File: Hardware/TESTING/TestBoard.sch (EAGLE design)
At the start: 91 parts, among them IC1 OP-AMP, J2 ISP, Q1 MOSFET_PCH-IRLML2244, U1 TAP_POINT, U10 MCP1755, U11 AD7280A, U12 ATMEGA328P_TQFP, U13 CH340C, U2 TAP_POINT, U3 TAP_POINT, U4 TAP_POINT, U5 TAP_POINT, U6 SINGLECELL, U7 SINGLECELL, U8 SINGLECELL, U9 SINGLECELL, Y1 16MHz

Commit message: Add spacious test board design
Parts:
- removed C14, C16, C17, C18, C20: 0.1uF, SparkFun-Capacitors:0.1UF-0603-25V-(+80/-20%)
- removed C19: 1.0uF, SparkFun-Capacitors:1.0UF-0603-16V-10%-X7R
- removed C21: 10nF, SparkFun-Capacitors:10NF-0603-50V-10%
- removed D8: BLUE, SparkFun-LED:LED-BLUE0603
- removed D9: 3A/10V/280mV, SparkFun-DiscreteSemi:DIODE-SCHOTTKY-BAT60A
- removed R33: 1k, SparkFun-Resistors:1KOHM-0603-1/10W-1%
- removed S2: TEST, SparkFun-Switches:MOMENTARY-SWITCH-SPST-SMD-5.2-TALL-REDUNDANT
- removed S3: Tall Switch, SparkFun-Switches:MOMENTARY-SWITCH-SPST-SMD-5.2-TALL-REDUNDANT
- removed U12: ATMEGA328P_TQFP, SparkFun-IC-Microcontroller:ATMEGA328P_TQFP
- removed U13: CH340C, SparkFun-IC-Comms:CH340C
- removed Y1: 16MHz, SparkFun-Clocks:RESONATOR-16MHZSMD_3.2X1.3
- added Q7: (no value), MTAES_V2_UniqueParts:AMP_MOSFET_NCH-2N7002K
- J1: device SparkFun-Connectors:USB_MICRO-B_HALF_PTH_MILL -> SparkFun-Connectors:CONN_10NO_SILK_PTH_FEMALE
- J2: value ISP -> (none); device SparkFun-Connectors:AVR_SPI_PROG_3X2TESTPOINTS -> SparkFun-Connectors:CONN_06NO_SILK_NO_POP
- Q1: value MOSFET_PCH-IRLML2244 -> (none); device SparkFun-DiscreteSemi:MOSFET_PCH-IRLML2244 -> MTAES_V2_UniqueParts:AMP_MOSFET_NCH-2N7002K
- R26: value 10k -> 1k; device SparkFun-Resistors:10KOHM-0603-1/10W-1% -> SparkFun-Resistors:1KOHM-0603-1/10W-1%
- R30: value 1k -> 10k; device SparkFun-Resistors:1KOHM-0603-1/10W-1% -> SparkFun-Resistors:10KOHM-0603-1/10W-1%
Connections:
- removed net !DTR: C14.1, U13.!DTR
- removed net AREF: C16.1, U12.AREF
- removed net D+: J1.D+, U13.UD+
- removed net D-: J1.D-, U13.UD-
- removed net LED1: D5.A, U12.PC0(ADC0)
- removed net LED2: D6.A, U12.PC1(ADC1)
- removed net LED3: D7.A, U12.PC2(ADC2)
- removed net LED4: D8.A, U12.PC3(ADC3)
- removed net N$4: U12.PB7(XTAL2/TOSC2), Y1.3
- removed net N$42: D7.C, R32.2
- removed net N$43: D6.C, R31.2
- removed net N$44: D5.C, R30.2
- removed net RX-I: U12.PD0(RXD), U13.TXO
- removed net SHLD: J1.SHIELD
- removed net TEST: D4.A, S2.1, U12.ADC6, U12.PD3(INT1)
- removed net TX-O: U12.PD1(TXD), U13.RXI
- removed net USBVCC: C18.1, C19.1, D9.A, J1.VBUS
- new net N$2: D7.C, Q7.D
- new net N$35: D4.A, R30.1
- new net N$36: J2.6
- net !CS: now also J1.10; no longer U12.PB2(SS/OC1B)
- net !CVNST: now also J1.5; no longer U12.ADC7
- net ALERT: now also J1.4; no longer U12.PD2(INT0)
- net CHARGE: now also J2.5, Q1.G
- net GND: now also D4.C, D5.C, J1.3, J2.3, Q1.S, Q7.S; no longer C16.2, C17.1, C18.2, C19.2, C20.2, C21.2, J1.GND, J2.6, Q1.G, R26.1, R30.1, R31.1, R32.1, R33.1, S3.1, U12.AGND, U12.GND, U13.GND, Y1.2
- net MISO: now also J1.7; no longer J2.1, U12.PB4(MISO)
- net MOSI: now also J1.9; no longer J2.4, U12.PB3(MOSI/OC2)
- net N$10: now also U6.-; no longer U8.-
- net N$3: now also D6.C, Q1.D; no longer U12.PB6(XTAL1/TOSC1), Y1.1
- net N$37: now also D5.A, R26.1; no longer D4.C, R26.2
- net N$38: now also D6.A, R31.1; no longer C21.1, U13.V3
- net N$39: now also D7.A, R32.1; no longer D8.C, R33.2
- net N$6: now also U8.-; no longer U6.-
- net N$8: now also U6.+; no longer U8.+
- net RESET: now also J1.6, J2.4, Q7.G; no longer C14.2, J2.5, S3.2, U12.PC6(/RESET)
- net SCLK: now also J1.8; no longer J2.3, U12.PB5(SCK)
- net VCC: now also J1.2, R26.2, R31.2, R32.2; no longer C17.2, C20.1, D9.C, S2.2, U12.AVCC, U12.VCC, U13.VCC
- net V_BATT: now also J1.1, J2.1, R30.2; no longer Q1.S
- net V_RAW: now also U8.+; no longer Q1.D, U6.+
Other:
- note removed: "ATmega328"
- note removed: "USB-to-Serial Converter"
- moved on the sheet: D4, D5, D6, D7, R26, R30, R31, R32, U6, U8

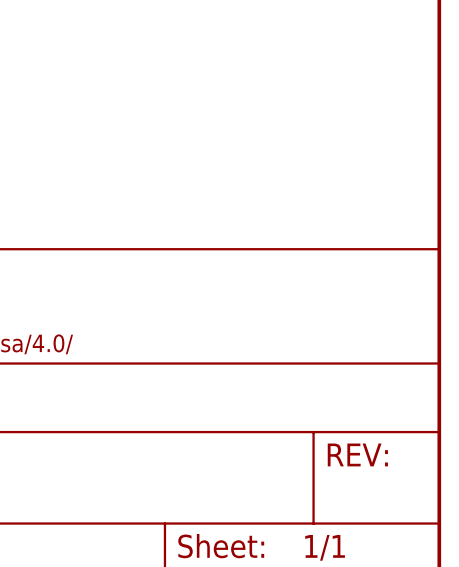
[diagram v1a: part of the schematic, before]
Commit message: Gerbered the testing board
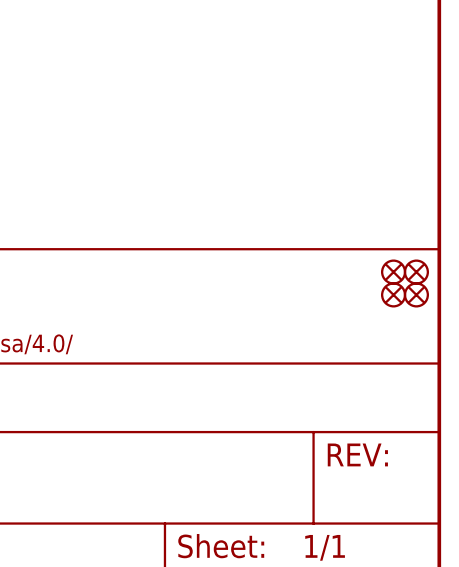
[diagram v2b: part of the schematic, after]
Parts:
- added FD1, FD2, FD3, FD4: FIDUCIALUFIDUCIAL, SparkFun-Aesthetics:FIDUCIALUFIDUCIAL
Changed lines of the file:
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@@
 <?xml version="1.0" encoding="utf-8"?>
 <!DOCTYPE eagle SYSTEM "eagle.dtd">
-<eagle version="9.2.0">
+<eagle version="9.1.3">
 <drawing>
 <settings>
-<setting alwaysvectorfont="no"/>
+<setting alwaysvectorfont="yes"/>
 <setting verticaltext="up"/>
 </settings>
@@
 <part name="SUPPLY17" library="SparkFun-PowerSymbols" deviceset="VCC" device=""/>
 <part name="SUPPLY18" library="SparkFun-PowerSymbols" deviceset="VCC" device=""/>
+<part name="FD1" library="SparkFun-Aesthetics" deviceset="FIDUCIAL" device="UFIDUCIAL"/>
+<part name="FD2" library="SparkFun-Aesthetics" deviceset="FIDUCIAL" device="UFIDUCIAL"/>
+<part name="FD3" library="SparkFun-Aesthetics" deviceset="FIDUCIAL" device="UFIDUCIAL"/>
+<part name="FD4" library="SparkFun-Aesthetics" deviceset="FIDUCIAL" device="UFIDUCIAL"/>
 </parts>
 <sheets>
@@
 <attribute name="VALUE" x="287.02" y="236.474" size="1.778" layer="96" align="bottom-center"/>
 </instance>
+<instance part="FD1" gate="G$1" x="429.26" y="33.02"/>
+<instance part="FD2" gate="G$1" x="426.72" y="33.02"/>
+<instance part="FD3" gate="G$1" x="426.72" y="30.48"/>
+<instance part="FD4" gate="G$1" x="429.26" y="30.48"/>
 </instances>
 <busses>

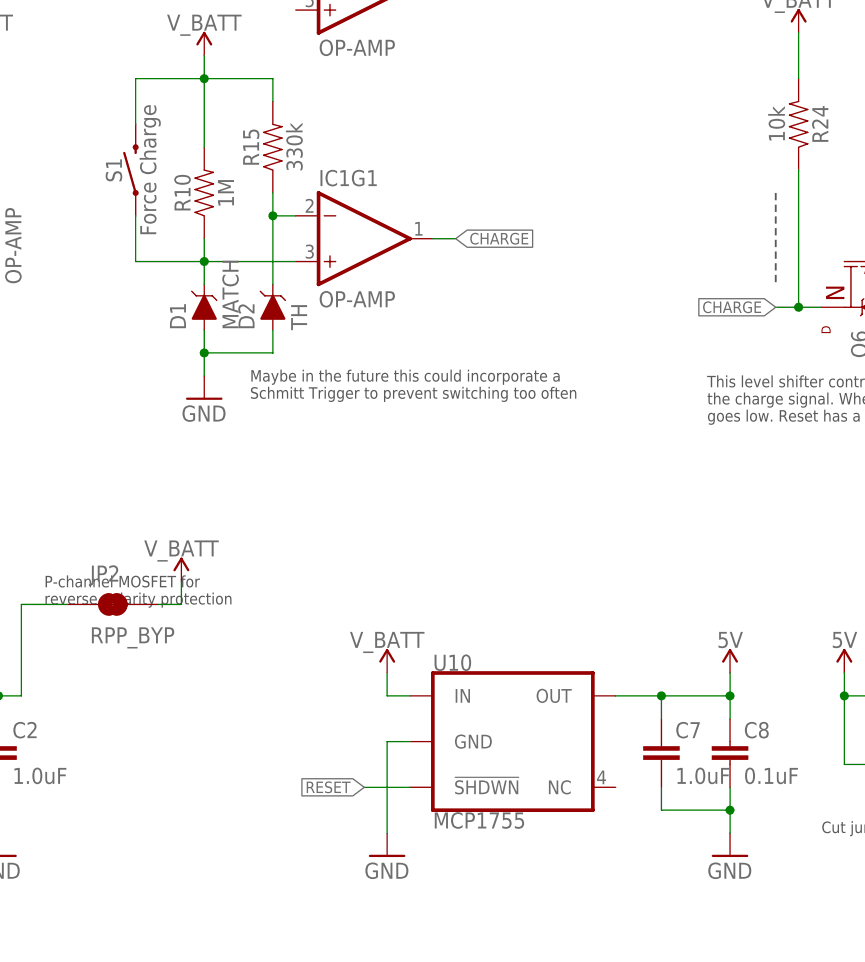
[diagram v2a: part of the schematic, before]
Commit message: Implement LV shutoff circuit changes in schematic
Switch to voltage-divider/zener comparator, change regulator enable to raw compararator output
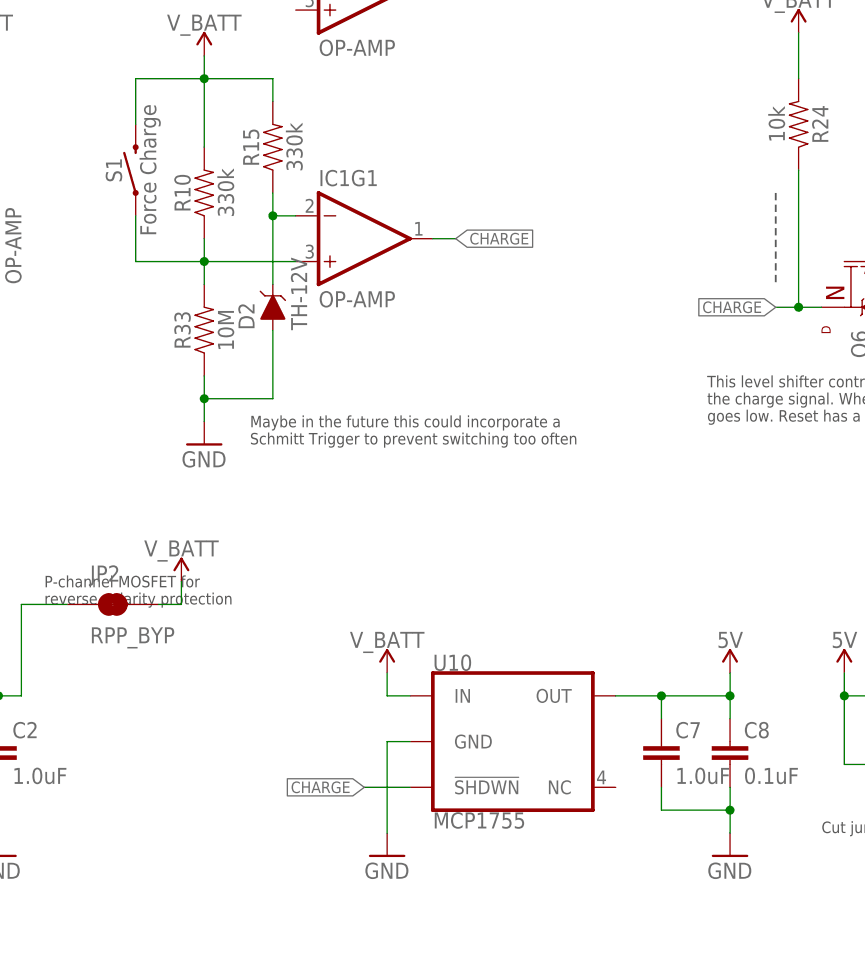
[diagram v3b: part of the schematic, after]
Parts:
- removed D1: MATCH, SparkFun-DiscreteSemi:DIODE-ZENER-MMBZ5233BLT1G
- added R33: 10M, SparkFun-Resistors:10MOHM-0603-1/10W-5%
- D2: value TH -> TH-12V
- R10: value 1M -> 330k; device SparkFun-Resistors:1MOHM-0603-1/4W-5% -> SparkFun-Resistors:330KOHM-0603-1/10W-1%
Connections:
- net CHARGE: now also U10.!SHDWN
- net GND: now also R33.1; no longer D1.A
- net N$40: now also R33.2; no longer D1.C
- net RESET: no longer U10.!SHDWN
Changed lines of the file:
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@@
 <part name="U2" library="BBLib" deviceset="TAP_POINT" device=""/>
 <part name="U1" library="BBLib" deviceset="TAP_POINT" device=""/>
-<part name="D2" library="SparkFun-DiscreteSemi" deviceset="DIODE-ZENER" device="-MMBZ5233BLT1G" value="TH"/>
+<part name="D2" library="SparkFun-DiscreteSemi" deviceset="DIODE-ZENER" device="-MMBZ5233BLT1G" value="TH-12V"/>
 <part name="IC1" library="SparkFun-IC-Amplifiers" deviceset="OPAMP-DUAL" device="U" value="OP-AMP"/>
-<part name="R10" library="SparkFun-Resistors" deviceset="1MOHM" device="-0603-1/4W-5%" value="1M"/>
-<part name="D1" library="SparkFun-DiscreteSemi" deviceset="DIODE-ZENER" device="-MMBZ5233BLT1G" value="MATCH"/>
 <part name="R15" library="SparkFun-Resistors" deviceset="330KOHM" device="-0603-1/10W-1%" value="330k"/>
 <part name="GND6" library="SparkFun" deviceset="GND" device=""/>
@@
 <part name="FD3" library="SparkFun-Aesthetics" deviceset="FIDUCIAL" device="UFIDUCIAL"/>
 <part name="FD4" library="SparkFun-Aesthetics" deviceset="FIDUCIAL" device="UFIDUCIAL"/>
+<part name="R10" library="SparkFun-Resistors" deviceset="330KOHM" device="-0603-1/10W-1%" value="330k"/>
+<part name="R33" library="SparkFun-Resistors" deviceset="10MOHM" device="-0603-1/10W-5%" value="10M"/>
 </parts>
 <sheets>
@@
 Zener diode clamps the inverting input, allowing the non-
 inverting input to be greater, yielding a HIGH voltage output</text>
-<text x="55.88" y="208.28" size="1.27" layer="97">Maybe in the future this could incorporate a
+<text x="55.88" y="203.2" size="1.27" layer="97">Maybe in the future this could incorporate a
 Schmitt Trigger to prevent switching too often</text>
 <text x="119.38" y="160.02" size="1.27" layer="97">Cut jumper is using USB-Serial</text>
@@
 <attribute name="VALUE" x="30.48" y="220.98" size="1.778" layer="95" font="vector" rot="R90"/>
 </instance>
-<instance part="R10" gate="G$1" x="50.8" y="231.14" rot="R90">
-<attribute name="NAME" x="49.276" y="231.14" size="1.778" layer="95" font="vector" rot="R90" align="bottom-center"/>
-<attribute name="VALUE" x="52.324" y="231.14" size="1.778" layer="96" font="vector" rot="R90" align="top-center"/>
-</instance>
-<instance part="D1" gate="G$1" x="50.8" y="218.44" rot="R90">
-<attribute name="NAME" x="48.768" y="215.9" size="1.778" layer="95" font="vector" rot="R90"/>
-<attribute name="VALUE" x="52.832" y="215.9" size="1.778" layer="96" font="vector" rot="R90" align="top-left"/>
-</instance>
 <instance part="R15" gate="G$1" x="58.42" y="236.22" rot="R90">
 <attribute name="NAME" x="56.896" y="236.22" size="1.778" layer="95" font="vector" rot="R90" align="bottom-center"/>
 <attribute name="VALUE" x="59.944" y="236.22" size="1.778" layer="96" font="vector" rot="R90" align="top-center"/>
 </instance>
-<instance part="GND6" gate="1" x="50.8" y="208.28">
-<attribute name="VALUE" x="48.26" y="205.74" size="1.778" layer="96"/>
+<instance part="GND6" gate="1" x="50.8" y="203.2">
+<attribute name="VALUE" x="48.26" y="200.66" size="1.778" layer="96"/>
 </instance>
 <instance part="GND2" gate="1" x="25.4" y="208.28">
@@
 <instance part="FD3" gate="G$1" x="426.72" y="30.48"/>
 <instance part="FD4" gate="G$1" x="429.26" y="30.48"/>
+<instance part="R10" gate="G$1" x="50.8" y="231.14" rot="R90">
+<attribute name="NAME" x="49.276" y="231.14" size="1.778" layer="95" font="vector" rot="R90" align="bottom-center"/>
+<attribute name="VALUE" x="52.324" y="231.14" size="1.778" layer="96" font="vector" rot="R90" align="top-center"/>
+</instance>
+<instance part="R33" gate="G$1" x="50.8" y="215.9" rot="R90"/>
 </instances>
 <busses>
@@
 </segment>
 <segment>
-<pinref part="D1" gate="G$1" pin="A"/>
-<wire x1="50.8" y1="215.9" x2="50.8" y2="213.36" width="0.1524" layer="91"/>
-<wire x1="50.8" y1="213.36" x2="58.42" y2="213.36" width="0.1524" layer="91"/>
+<wire x1="50.8" y1="210.82" x2="50.8" y2="208.28" width="0.1524" layer="91"/>
+<wire x1="50.8" y1="208.28" x2="58.42" y2="208.28" width="0.1524" layer="91"/>
 <pinref part="D2" gate="G$1" pin="A"/>
-<wire x1="58.42" y1="213.36" x2="58.42" y2="215.9" width="0.1524" layer="91"/>
+<wire x1="58.42" y1="208.28" x2="58.42" y2="215.9" width="0.1524" layer="91"/>
 <pinref part="GND6" gate="1" pin="GND"/>
-<wire x1="50.8" y1="213.36" x2="50.8" y2="210.82" width="0.1524" layer="91"/>
-<junction x="50.8" y="213.36"/>
+<wire x1="50.8" y1="208.28" x2="50.8" y2="205.74" width="0.1524" layer="91"/>
+<junction x="50.8" y="208.28"/>
+<pinref part="R33" gate="G$1" pin="1"/>
 </segment>
 <segment>
@@
 </segment>
 <segment>
-<pinref part="U10" gate="G$1" pin="!SHDWN"/>
-<wire x1="73.66" y1="165.1" x2="68.58" y2="165.1" width="0.1524" layer="91"/>
-<label x="68.58" y="165.1" size="1.27" layer="95" rot="R180" xref="yes"/>
-</segment>
-<segment>
 <pinref part="J2" gate="G$1" pin="4"/>
 <wire x1="187.96" y1="223.52" x2="180.34" y2="223.52" width="0.1524" layer="91"/>
@@
 <pinref part="IC1" gate="G1" pin="+IN"/>
 <wire x1="60.96" y1="223.52" x2="50.8" y2="223.52" width="0.1524" layer="91"/>
-<pinref part="R10" gate="G$1" pin="1"/>
 <wire x1="50.8" y1="223.52" x2="50.8" y2="226.06" width="0.1524" layer="91"/>
-<pinref part="D1" gate="G$1" pin="C"/>
 <wire x1="50.8" y1="220.98" x2="50.8" y2="223.52" width="0.1524" layer="91"/>
 <junction x="50.8" y="223.52"/>
@@
 <wire x1="43.18" y1="228.6" x2="43.18" y2="223.52" width="0.1524" layer="91"/>
 <wire x1="43.18" y1="223.52" x2="50.8" y2="223.52" width="0.1524" layer="91"/>
+<pinref part="R10" gate="G$1" pin="1"/>
+<pinref part="R33" gate="G$1" pin="2"/>
 </segment>
 </net>
@@
 <label x="261.62" y="200.66" size="1.27" layer="95" rot="R180" xref="yes"/>
 </segment>
+<segment>
+<pinref part="U10" gate="G$1" pin="!SHDWN"/>
+<wire x1="73.66" y1="165.1" x2="68.58" y2="165.1" width="0.1524" layer="91"/>
+<label x="68.58" y="165.1" size="1.27" layer="95" rot="R180" xref="yes"/>
+</segment>
 </net>
 <net name="V_BATT" class="0">
@@
 </segment>
 <segment>
-<pinref part="R10" gate="G$1" pin="2"/>
 <wire x1="50.8" y1="236.22" x2="50.8" y2="243.84" width="0.1524" layer="91"/>
 <pinref part="R15" gate="G$1" pin="2"/>
@@
 <wire x1="43.18" y1="238.76" x2="43.18" y2="243.84" width="0.1524" layer="91"/>
 <wire x1="43.18" y1="243.84" x2="50.8" y2="243.84" width="0.1524" layer="91"/>
-</segment>
-<segment>
+<pinref part="R10" gate="G$1" pin="2"/>
+</segment>
+<segment>
